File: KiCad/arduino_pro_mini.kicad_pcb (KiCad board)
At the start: 4 copper layers, 22 parts, among them IC101 ATMEGA328P-AU, IC102 UA78M05CDCYR, Y401 16Mhz

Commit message: Initial scheme
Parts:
- removed C404, C405: 100nF, Capacitor_SMD:C_0402_1005Metric
- removed C408, C409: 15p, Capacitor_SMD:C_0402_1005Metric
- removed D201: 1N5819HW-7-F, Diode_SMD:D_SOD-123
- removed D207, D401: LED, LED_SMD:LED_0603_1608Metric
- removed R401: 1kR, Resistor_SMD:R_0805_2012Metric
- removed R407: 47R, Resistor_SMD:R_0402_1005Metric
- removed Y401: 16Mhz, Crystal:Crystal_SMD_3225-4Pin_3.2x2.5mm
- added C107: 100nF, Capacitor_SMD:C_0402_1005Metric, F.Cu at (128.2, 55.2)
- added C108: 15p, Capacitor_SMD:C_0402_1005Metric, F.Cu at (128.2, 57.2)
- added C109: 15p, Capacitor_SMD:C_0402_1005Metric, F.Cu at (128.2, 59.1)
- added C110: 100nF, Capacitor_SMD:C_0402_1005Metric, F.Cu at (128.2, 61.1)
- added D101: 1N5819HW-7-F, Diode_SMD:D_SOD-123, F.Cu at (132.6, 55.9)
- added D102: LED, LED_SMD:LED_0603_1608Metric, F.Cu at (131.7, 63.4)
- added D103: LED, LED_SMD:LED_0603_1608Metric, F.Cu at (131.7, 66.0)
- added J101: Conn_01x06_Pin, Connector_PinHeader_2.54mm:PinHeader_1x06_P2.54mm_Vertical, F.Cu at (129.1, 29.6)
- added J102: Conn_01x15_Pin, Connector_PinHeader_2.54mm:PinHeader_1x15_P2.54mm_Vertical, F.Cu at (119.9, 29.6)
- added J103: Conn_01x15_Pin, Connector_PinHeader_2.54mm:PinHeader_1x15_P2.54mm_Vertical, F.Cu at (124.5, 29.6)
- added J104: Conn_02x03_Odd_Even, Connector_PinHeader_2.54mm:PinHeader_2x03_P2.54mm_Vertical, F.Cu at (129.1, 46.8)
- added R103: 1kR, Resistor_SMD:R_0805_2012Metric, F.Cu at (133.6, 28.7)
- added R104: 1kR, Resistor_SMD:R_0805_2012Metric, F.Cu at (133.6, 31.7)
- added R105: 1kR, Resistor_SMD:R_0805_2012Metric, F.Cu at (133.6, 34.6)
- added R106: 1kR, Resistor_SMD:R_0805_2012Metric, F.Cu at (133.6, 37.6)
- added Y101: 16Mhz, Crystal:Crystal_SMD_3225-4Pin_3.2x2.5mm, F.Cu at (132.3, 59.8)
- C102: value 10uF_P -> 100nF; footprint Capacitor_Tantalum_SMD:CP_EIA-3216-18_Kemet-A -> Capacitor_SMD:C_0402_1005Metric
- C105: value 100nF -> 10uF_P; footprint Capacitor_SMD:C_0402_1005Metric -> Capacitor_Tantalum_SMD:CP_EIA-3216-18_Kemet-A
- IC101: value ATMEGA328P-AU -> UA78M05CDCYR; footprint atmega328p:QFP80P900X900X120-32N -> atmega328p:SOT230P700X180-4N
- IC102: value UA78M05CDCYR -> ATMEGA328P-AU; footprint atmega328p:SOT230P700X180-4N -> atmega328p:QFP80P900X900X120-32N
- R102: value 1kR -> 47R; footprint Resistor_SMD:R_0805_2012Metric -> Resistor_SMD:R_0402_1005Metric
- moved JP101 17.6 mm to (63.2, 43.0)
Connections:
- C101 pad 1: VIN -> +5V
- C102 pad 1: +5V_LDO -> +5V
- C103 pad 1: /AREF -> +5V
- C104 pad 1: +5V -> VIN
- C105 pad 1: +5V -> +5V_LDO
- C106 pad 1: +5V -> +5V_LDO
- IC101 pad 1: unconnected-(IC101-(PCINT19/OC2B/INT1)_PD3-Pad1) -> VIN
- IC101 pad 2: unconnected-(IC101-(PCINT20/XCK/T0)_PD4-Pad2) -> GND
- IC101 pad 3: GND -> +5V_LDO
- IC101 pad 4: +5V -> GND
- IC102 pad 1: VIN -> D3
- IC102 pad 2: GND -> D4
- IC102 pad 3: +5V_LDO -> GND
- IC102 pad 4: GND -> +5V
- R102 pad 1: Net-(D401-K) -> XTAL_OUT
- R102 pad 2: GND -> Net-(C109-Pad1)

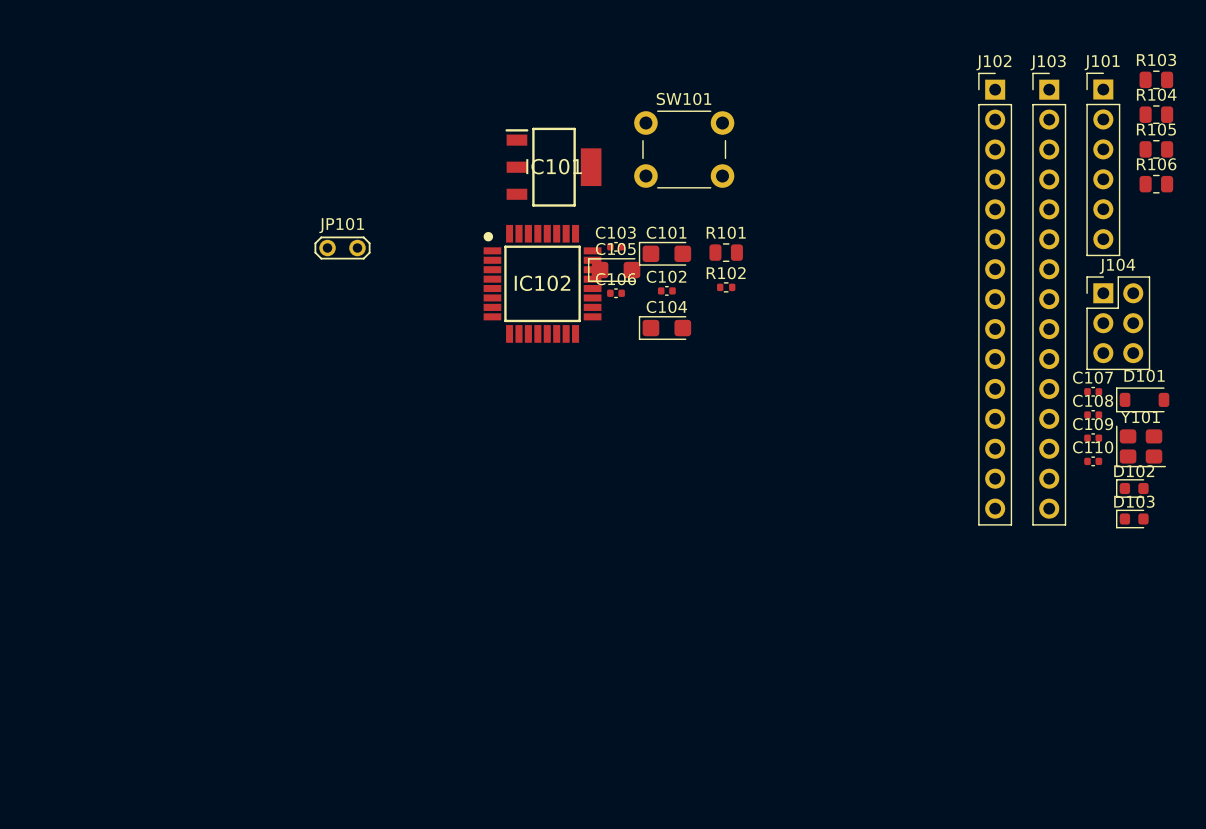
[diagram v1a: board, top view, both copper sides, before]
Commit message: first pcb component placement
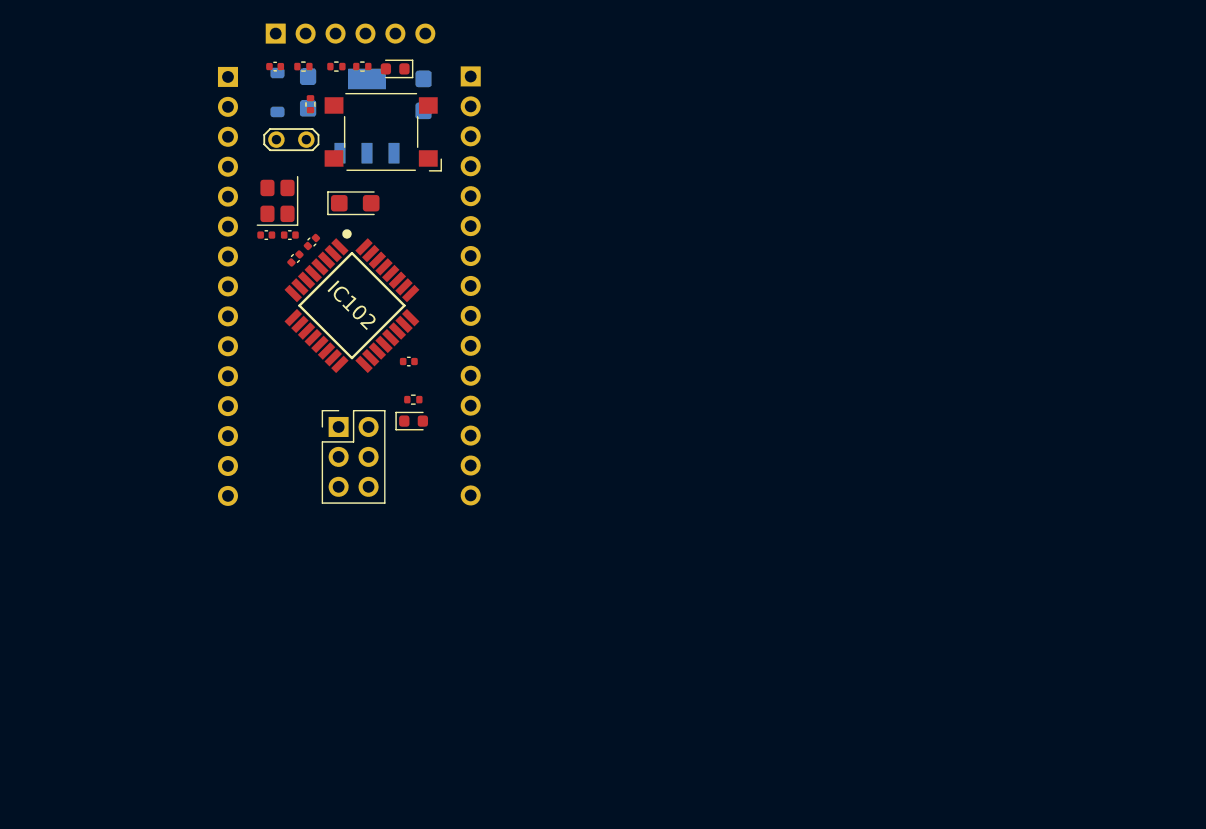
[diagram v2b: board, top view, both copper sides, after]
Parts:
- removed C110: 100nF, Capacitor_SMD:C_0402_1005Metric
- removed R106: 1kR, Resistor_SMD:R_0805_2012Metric
- C104, C105, D101, IC101, J101, J102, J103: moved to B.Cu
- C107: value 100nF -> 15p
- C109: value 15p -> 100nF
- R101, R103, R104, R105: footprint Resistor_SMD:R_0805_2012Metric -> Resistor_SMD:R_0402_1005Metric
- R102: value 47R -> 1kR
- SW101: value ~ -> SW_Omron_B3FS; footprint atmega328p:SW_PUSH_6mm_H5mm -> Button_Switch_SMD:SW_SPST_Omron_B3FS-100xP
- moved D101 78.1 mm to (59.0, 29.8), turned to -90 degrees
- moved C109 76.3 mm to (58.8, 27.6)
- moved Y101 76.2 mm to (59.0, 39.0), turned to 90 degrees
- moved R103 72.4 mm to (61.2, 27.6), turned to 180 degrees
- moved D102 72.1 mm to (69.0, 27.8), turned to 180 degrees
- moved C108 71.8 mm to (58.0, 41.9), turned to 180 degrees
- moved R104 71.8 mm to (61.8, 30.8), turned to 90 degrees
- moved J101 70.4 mm to (58.9, 24.8), turned to -90 degrees
- moved C107 69.5 mm to (60.0, 41.9)
- moved R105 66.5 mm to (70.5, 55.9)
- moved J104 65.9 mm to (64.2, 58.2)
- moved J102 65.1 mm to (54.8, 28.5), turned to 180 degrees
- moved D103 61.7 mm to (70.6, 57.7)
- moved J103 49.1 mm to (75.4, 28.4), turned to 180 degrees
- moved R102 38.0 mm to (64.0, 27.6), turned to 180 degrees
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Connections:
- C106 pad 1: +5V_LDO -> AREF
- C107 pad 1: AREF -> XTAL_IN
- C108 pad 1: XTAL_IN -> XTAL_OUT
- C109 pad 1: Net-(C109-Pad1) -> RESET
- C109 pad 2: GND -> /DTR
- R102 pad 1: XTAL_OUT -> /TXD
- R102 pad 2: Net-(C109-Pad1) -> D0_RX
- R103 pad 1: /TXD -> /RXD
- R103 pad 2: D0_RX -> D1_TX
- R104 pad 1: /RXD -> +5V
- R104 pad 2: D1_TX -> RESET
- R105 pad 1: +5V -> Net-(D103-K)
- R105 pad 2: RESET -> GND
- SW101 pad 1: RESET -> GND
- SW101 pad 2: GND -> RESET
- Y101 pad 3: Net-(C109-Pad1) -> XTAL_OUT

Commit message: Board outline
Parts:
- C101: moved to B.Cu
- moved D102 35.3 mm to (44.2, 53.0), turned to 0 degrees
- moved R104 33.4 mm to (42.8, 58.2)
- moved C105 33.0 mm to (46.2, 59.0), turned to -90 degrees
- moved D101 32.9 mm to (43.8, 59.0), turned to 90 degrees
- moved C104 32.5 mm to (56.5, 58.9)
- moved R101 31.8 mm to (47.0, 53.0), turned to 180 degrees
- moved IC101 30.5 mm to (51.5, 58.2)
- moved C102 30.1 mm to (46.0, 68.0), turned to 135 degrees
- moved C103 29.9 mm to (44.8, 69.2), turned to 135 degrees
- moved J101 29.4 mm to (43.6, 50.0)
- moved IC102 29.4 mm to (50.0, 73.0)
- moved C106 29.3 mm to (55.1, 77.8)
- moved D103 29.3 mm to (55.5, 82.8)
- moved R105 29.3 mm to (55.5, 81.0)
- moved J104 29.3 mm to (48.7, 83.0)
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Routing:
- added copper zone on In1.Cu, net GND
- added copper zone on In2.Cu, net GND
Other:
- board outline added: 25 x 42.5 mm

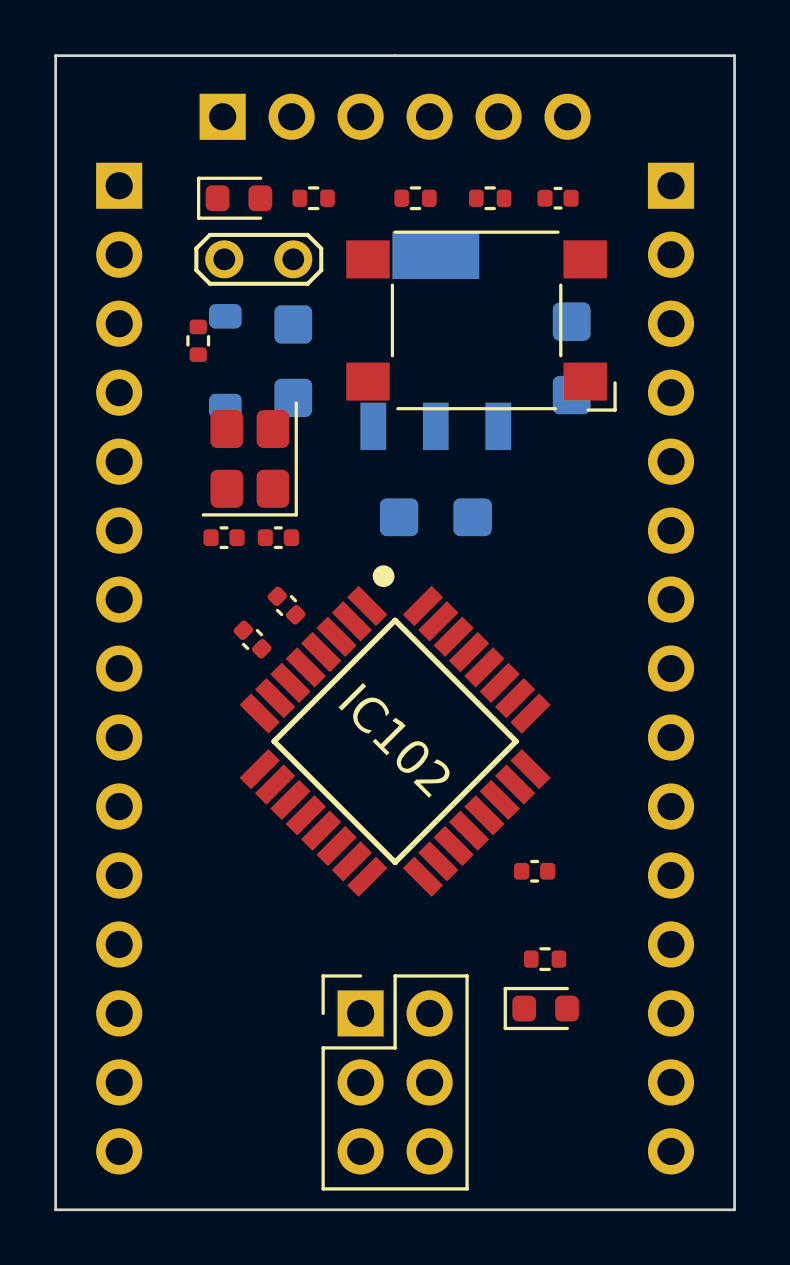
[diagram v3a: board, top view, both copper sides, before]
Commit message: Add signal traces to PCB
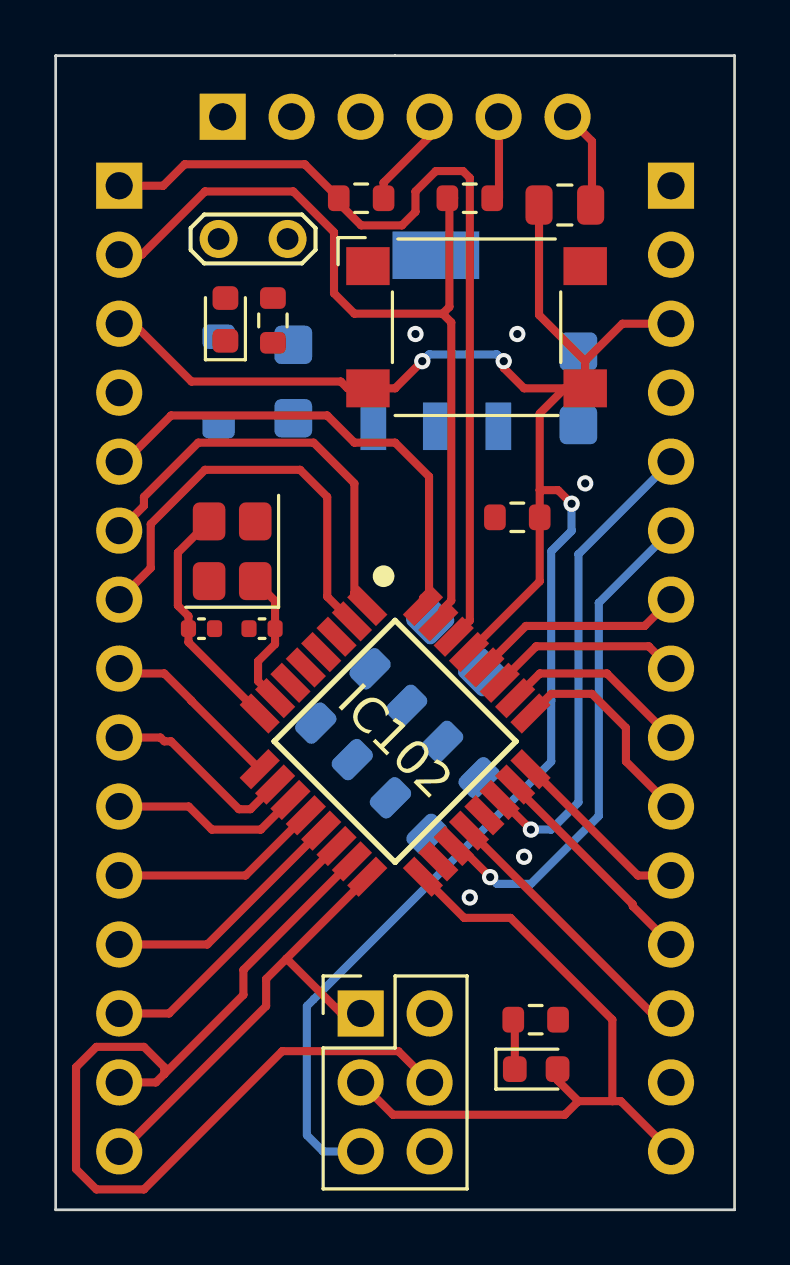
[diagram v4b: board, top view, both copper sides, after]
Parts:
- added C110: 100nF, Capacitor_SMD:C_0805_2012Metric, F.Cu at (56.2, 53.2)
- C102, C103: footprint Capacitor_SMD:C_0402_1005Metric -> Capacitor_SMD:C_0805_2012Metric; moved to B.Cu
- C104: value 10uF_P -> 100nF; footprint Capacitor_Tantalum_SMD:CP_EIA-3216-18_Kemet-A -> Capacitor_SMD:C_0805_2012Metric
- C106: value 100nF -> 10uF_P; footprint Capacitor_SMD:C_0402_1005Metric -> Capacitor_Tantalum_SMD:CP_EIA-3216-18_Kemet-A; moved to B.Cu
- C107: value 15p -> 100nF; footprint Capacitor_SMD:C_0402_1005Metric -> Capacitor_SMD:C_0805_2012Metric; moved to B.Cu
- C109: value 100nF -> 15p
- R101, R102, R103, R104, R105: footprint Resistor_SMD:R_0402_1005Metric -> Resistor_SMD:R_0603_1608Metric
- moved C109 20.6 mm to (42.9, 68.8)
- moved C106 20.1 mm to (46.2, 59.8), turned to -90 degrees
- moved C104 13.9 mm to (49.8, 71.0), turned to -45 degrees
- moved R104 13.4 mm to (54.5, 64.8), turned to 0 degrees
- moved C107 10.6 mm to (52.4, 73.7), turned to 135 degrees
- moved C105 10.5 mm to (56.8, 60.0)
- moved C103 8.68 mm to (50.5, 75.8)
- moved C102 5.30 mm to (47.8, 73.0), turned to -45 degrees
- moved C101 4.81 mm to (52.2, 69.5), turned to -45 degrees
- moved R101 4.74 mm to (45.5, 57.5), turned to -90 degrees
- moved D102 4.49 mm to (43.8, 57.5), turned to 90 degrees
- moved C108 3.63 mm to (45.1, 68.8)
- moved Y101 3.46 mm to (44.0, 66.0)
- moved R105 2.26 mm to (55.2, 83.2)
- moved D103 2.26 mm to (55.2, 85.1)
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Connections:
- C104 pad 1: VIN -> +5V
- C105 pad 1: +5V_LDO -> VIN
- C106 pad 1: AREF -> +5V_LDO
- C107 pad 1: XTAL_IN -> AREF
- C108 pad 1: XTAL_OUT -> XTAL_IN
- C109 pad 1: RESET -> XTAL_OUT
- C109 pad 2: /DTR -> GND
- J102 pad 1: D1_TX -> D0_RX
- J102 pad 2: D0_RX -> D1_TX
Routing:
- net RESET: track 0.00 -> 73.6 mm, vias 0 -> 3
- net D11_MOSI: track 0.00 -> 36.3 mm
- net D0_RX: track 0.00 -> 33.4 mm
- net D1_TX: track 0.00 -> 32.1 mm
- net D13_SCK: track 0.00 -> 26.5 mm
- net A6: track 0.00 -> 18.6 mm, vias 0 -> 1
- net D12_MISO: track 0.00 -> 18.2 mm
- net D2: track 0.00 -> 17.9 mm
- net A7: track 0.00 -> 17.7 mm, vias 0 -> 1
- net D4: track 0.00 -> 16.0 mm
- net D3: track 0.00 -> 15.5 mm
- net D10: track 0.00 -> 10.6 mm
- net AREF: track 0.00 -> 10.2 mm
- net D9: track 0.00 -> 9.17 mm
- net XTAL_OUT: track 0.00 -> 8.84 mm
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
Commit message: All connected
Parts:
- C108, C109: footprint Capacitor_SMD:C_0402_1005Metric -> Capacitor_SMD:C_0603_1608Metric
- moved C108 2.87 mm to (46.8, 66.5), turned to 90 degrees
- moved C106 1.25 mm to (46.2, 58.5)
- moved D101 1.25 mm to (43.5, 58.5)
- moved C109 0.39 mm to (43.2, 69.0)
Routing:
- net +5V: track 0.00 -> 74.5 mm, vias 0 -> 4
- net GND: track 0.00 -> 36.9 mm, vias 5 -> 30
- net VIN: track 0.00 -> 12.7 mm
- net +5V_LDO: track 0.00 -> 11.1 mm
- net AREF: track 10.2 -> 13.4 mm, vias 0 -> 1
- net Net-(D102-A): track 0.00 -> 2.48 mm
- net Net-(D101-A): track 0.00 -> 2.35 mm
- net XTAL_IN: track 5.13 -> 7.28 mm
- added copper zone on B.Cu, net GND
- added copper zone on F.Cu, net GND
